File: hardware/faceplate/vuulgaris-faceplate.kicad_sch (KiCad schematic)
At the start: 1 part, among them J1 2x5 SMD box header -- PLACEHO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

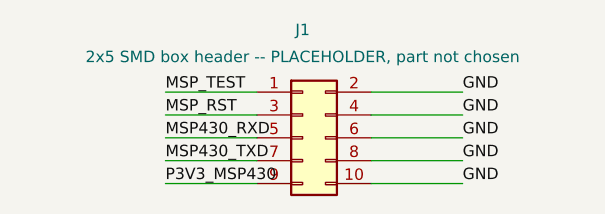
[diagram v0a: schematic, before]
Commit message: faceplate: J1 is the hanxia HX JN2.54-2x5P TP H8.9 (C41376028)
The cable header's placeholder (KiCad's generic SMD box header) is replaced by
a real part. It is Extended: JLC's Basic filter returns no SMD 2x5 box header
at all. Of the SMD ones, this has the most JLC stock (4715) and a drawing with
a recommended land pattern; the runner-up, XFCN BH254VS-10P (C492446), is
10.5mm tall against a 10mm gap. This one seats at 9.60mm.

New footprint IDC-SMD_10P-P2.54_C41376028 in the shared library, from hanxia's
drawing (datasheets/hanxia-HX-JN2.54-2x5P-TP-H8.9.pdf, now in
fetch-datasheets.sh), read at 6x: pads 1.02 x 4.65 on 2.54mm pitch, 11.50
overall (row centres +-3.425); body 20.30 x 8.90; leg tips 10.20 across; key
slot 4.50 wide. Fab carries the body and the leg tips, which is what
panelcheck measures against the cutout. The drawing marks pin 1 only by a
triangle on the key wall, so pin 1 is on the key-side row at that end -- the
same convention as KiCad's DIN 41651 footprint and main-board J12. Still to be
confirmed with a real ribbon before ordering (README section 5).

Board: J1 swapped by a one-off pcbnew script using mkboard.py's rule (pad
centroid on the cutout centre, pad 1 the way J12's lies, on B.Cu) and its
four GND row joins redrawn for the new pads. Diffed against HEAD: J1 and
those four segments are the only changes; the centroid is where it was.

Checked: netcheck 10/10, 0 unintended; boardcheck 0/0/0; DRC 0 errors, 0
warnings (the stock footprint's warning is gone); panelcheck 6 OK -- body and
legs 20.40 x 10.30 in the 24 x 12 cutout, tightest side 0.85mm.
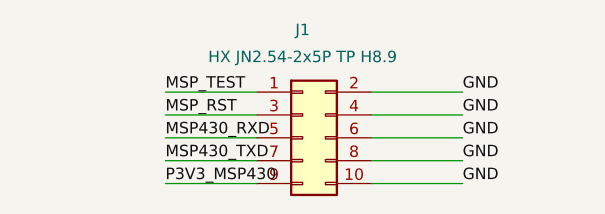
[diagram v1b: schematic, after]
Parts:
- J1: value 2x5 SMD box header -- PLACEHOLDER, part not chosen -> HX JN2.54-2x5P TP H8.9; footprint Connector_IDC:IDC-Header_2x05_P2.54mm_Vertical_SMD -> vuulgaris:IDC-SMD_10P-P2.54_C41376028
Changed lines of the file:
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@@
     (in_bom yes) (on_board yes) (dnp no)
     (property "Reference" "J1" (at 100 88 0) (effects (font (size 1.27 1.27))))
-    (property "Value" "2x5 SMD box header -- PLACEHOLDER, part not chosen" (at 100 91 0) (effects (font (size 1.27 1.27))))
-    (property "Footprint" "Connector_IDC:IDC-Header_2x05_P2.54mm_Vertical_SMD" (at 100 100 0) (effects (font (size 1.27 1.27)) hide))
+    (property "Value" "HX JN2.54-2x5P TP H8.9" (at 100 91 0) (effects (font (size 1.27 1.27))))
+    (property "Footprint" "vuulgaris:IDC-SMD_10P-P2.54_C41376028" (at 100 100 0) (effects (font (size 1.27 1.27)) hide))
     (property "Datasheet" "" (at 100 100 0) (effects (font (size 1.27 1.27)) hide))
     (pin "1")

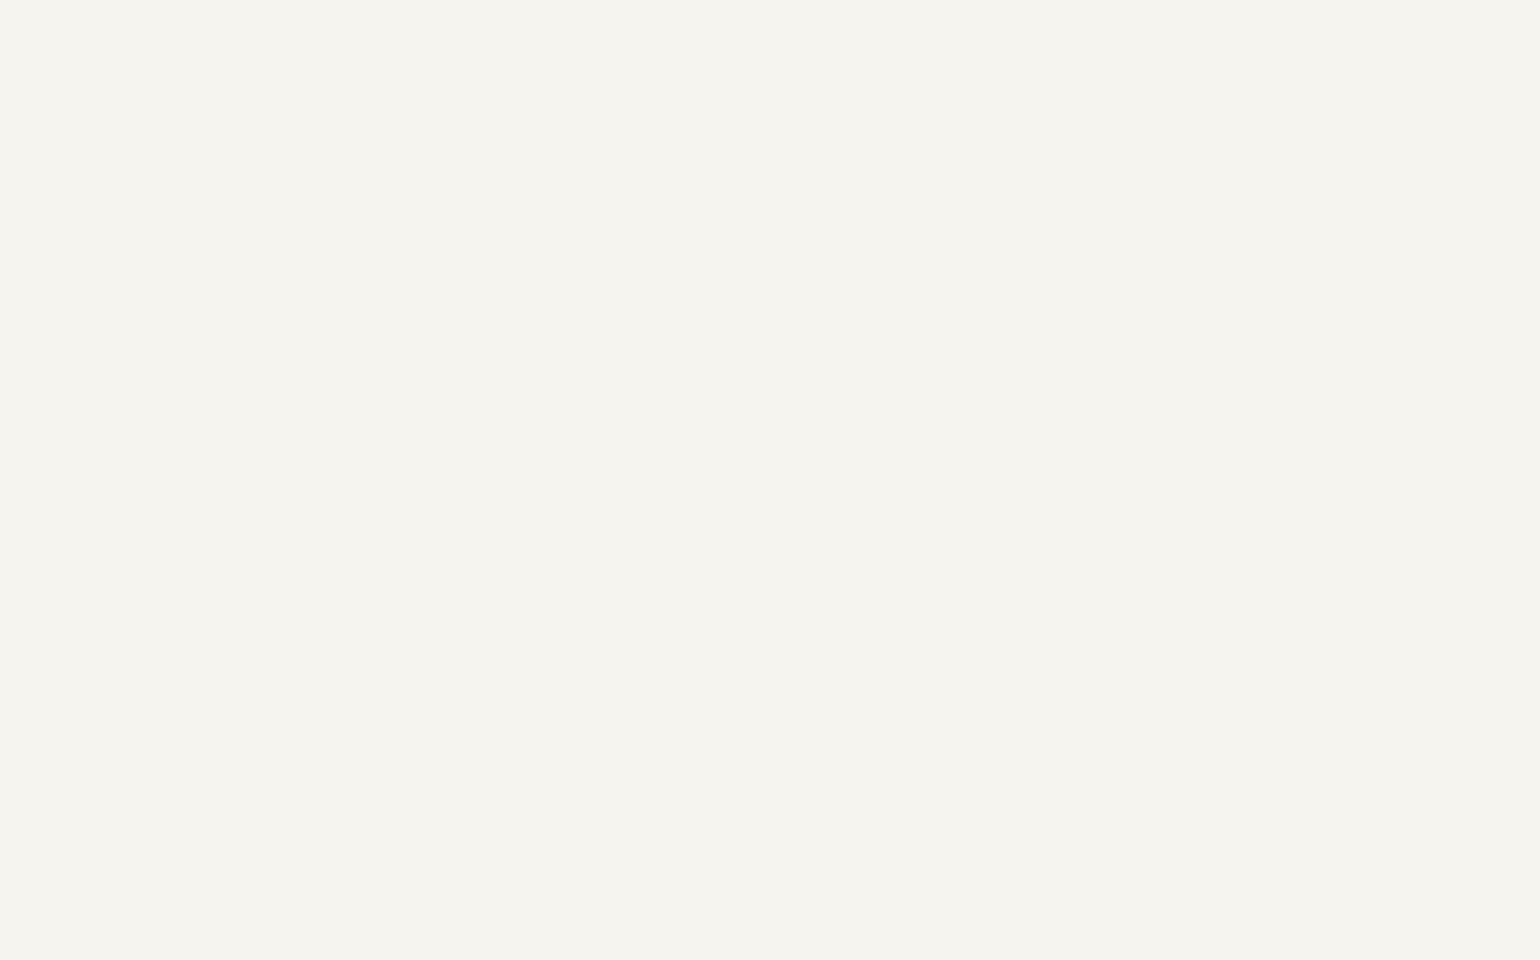
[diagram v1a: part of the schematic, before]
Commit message: faceplate: U1 with its supply, VREG and RST/TEST network
U1 (MSP430FR2675TPT) enters the schematic with the parts TI's reference
circuits call for around its supply and system pins. design.py is now
arranged by block, each saying which figure it came from.

From a TI reference circuit (SLASEO5D):
- C1 10uF + C2 100nF on DVCC/DVSS: section 10.1.1, Figure 10-1. DVCC is
  P3V3_MSP430 straight off the cable; the figure has nothing between supply
  and pin but the two capacitors.
- C3 1uF on VREG (pin 31): section 4, notes under Figure 4-1, "1 uF, with a
  maximum ESR of <=200 mohm".
- R1 47k pull-up + C4 1nF on RST/NMI/SBWTDIO (pin 2): Figure 10-4, the
  Spy-Bi-Wire connection, "upper limit for C1 is 1.1 nF". Required, not just
  tidy: MSP_RST is driven by the main board's MCP23017, high-Z at power-up.
- TEST/SBWTCK (pin 3): nothing. Figure 10-4 wires it straight to the tool;
  Table 7-4, unused TEST: "Open. This pin always has an internal pulldown
  enabled". pin-allocation.md asked for an external pulldown; corrected to
  TI's text in this commit.

Not from a reference circuit: package sizes (0603, 0805 at 1uF and up) follow
the main board's standard. TI's hardware tools guide (SLAU278) was not
fetched; the device datasheet's own Figure 10-4 gives the SBW values for this
part.

Checked: mksch -> netcheck 25/25, 0 unintended, 7 nets. DRC 0/0 and
panelcheck unchanged (the board is not touched). boardcheck parity lists
U1 and C1-C4/R1 as absent from the board -- expected until layout; nothing
is on a net netmap did not ask for.
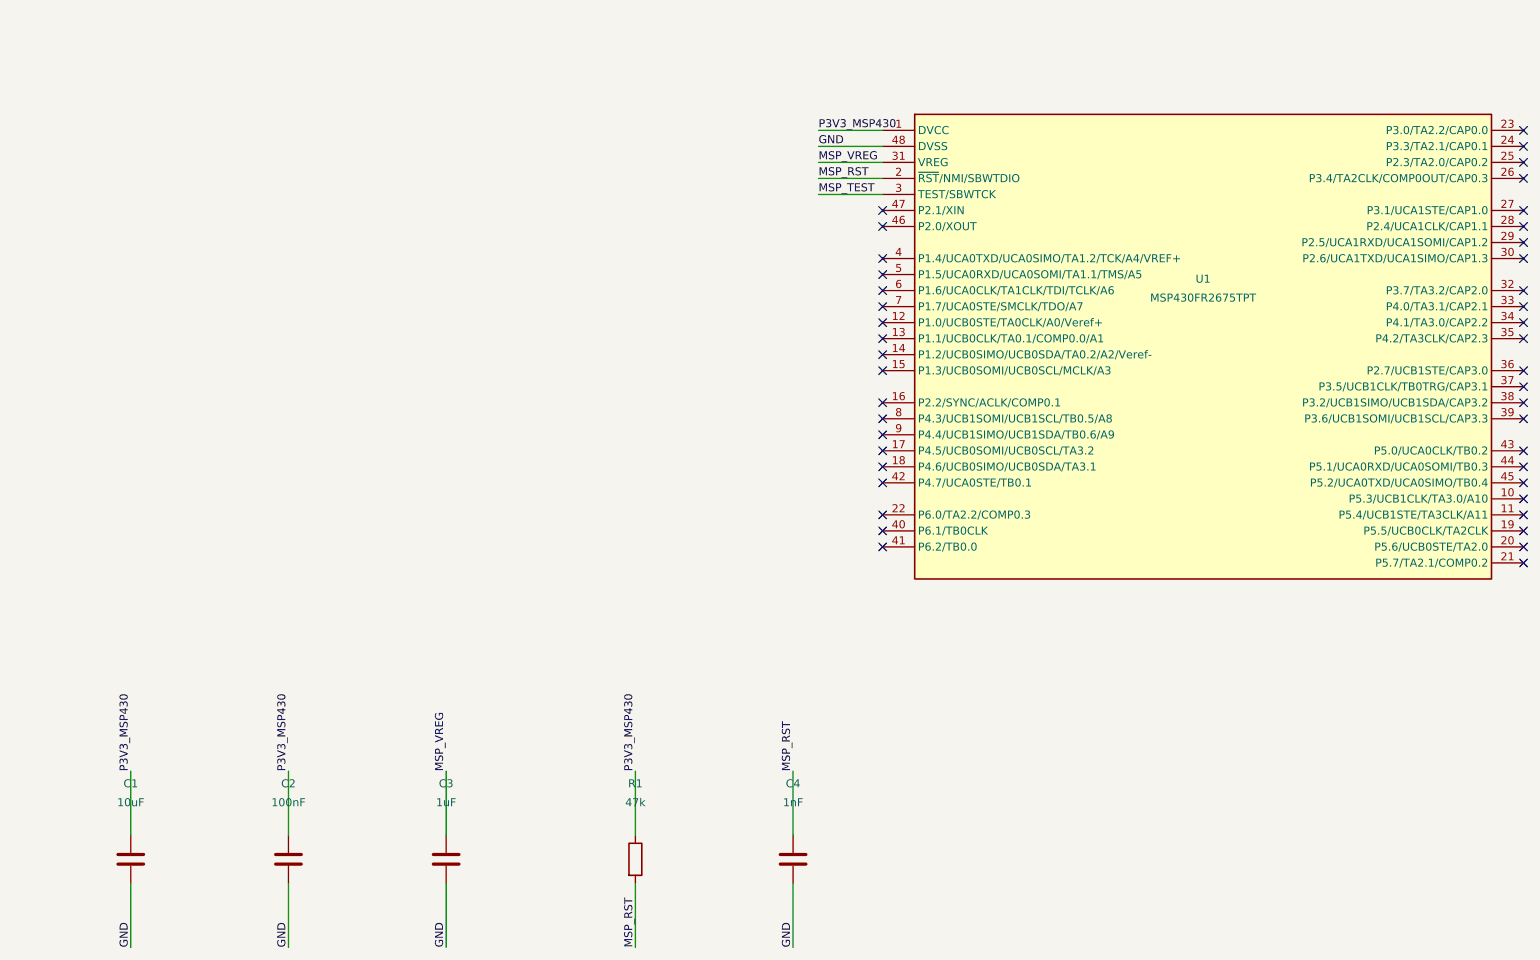
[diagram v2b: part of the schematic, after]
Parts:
- added C1: 10uF, vuulgaris:C0805, symbol vuulgaris:C
- added C2: 100nF, vuulgaris:C0603, symbol vuulgaris:C
- added C3: 1uF, vuulgaris:C0805, symbol vuulgaris:C
- added C4: 1nF, vuulgaris:C0603, symbol vuulgaris:C
- added R1: 47k, vuulgaris:R0603, symbol vuulgaris:R
- added U1: MSP430FR2675TPT, vuulgaris:LQFP-48_7x7mm_P0.5mm_PT0048A, symbol vuulgaris:MSP430FR2675TPT
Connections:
- net GND: now also C1.2, C2.2, C3.2, C4.2, U1.48 (DVSS)
- net MSP_RST: now also C4.1, R1.2, U1.2 (~{RST}/NMI/SBWTDIO)
- net MSP_TEST: now also U1.3 (TEST/SBWTCK)
- net P3V3_MSP430: now also C1.1, C2.1, R1.1, U1.1 (DVCC)
- new net MSP_VREG: C3.1, U1.31 (VREG)
- no-connect marks 0 -> 43
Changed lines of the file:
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@@
 (kicad_sch (version 20221206) (generator eeschema)
   (paper "A1")
+  (symbol (lib_id "vuulgaris:C") (at 160 300 0) (unit 1)
+    (in_bom yes) (on_board yes) (dnp no)
+    (property "Reference" "C1" (at 160 288 0) (effects (font (size 1.27 1.27))))
+    (property "Value" "10uF" (at 160 291 0) (effects (font (size 1.27 1.27))))
+    (property "Footprint" "vuulgaris:C0805" (at 160 300 0) (effects (font (size 1.27 1.27)) hide))
+    (property "Datasheet" "" (at 160 300 0) (effects (font (size 1.27 1.27)) hide))
+    (pin "1")
+    (pin "2")
+  )
+  (symbol (lib_id "vuulgaris:C") (at 185 300 0) (unit 1)
+    (in_bom yes) (on_board yes) (dnp no)
+    (property "Reference" "C2" (at 185 288 0) (effects (font (size 1.27 1.27))))
+    (property "Value" "100nF" (at 185 291 0) (effects (font (size 1.27 1.27))))
+    (property "Footprint" "vuulgaris:C0603" (at 185 300 0) (effects (font (size 1.27 1.27)) hide))
+    (property "Datasheet" "" (at 185 300 0) (effects (font (size 1.27 1.27)) hide))
+    (pin "1")
+    (pin "2")
+  )
+  (symbol (lib_id "vuulgaris:C") (at 210 300 0) (unit 1)
+    (in_bom yes) (on_board yes) (dnp no)
+    (property "Reference" "C3" (at 210 288 0) (effects (font (size 1.27 1.27))))
+    (property "Value" "1uF" (at 210 291 0) (effects (font (size 1.27 1.27))))
+    (property "Footprint" "vuulgaris:C0805" (at 210 300 0) (effects (font (size 1.27 1.27)) hide))
+    (property "Datasheet" "" (at 210 300 0) (effects (font (size 1.27 1.27)) hide))
+    (pin "1")
+    (pin "2")
+  )
+  (symbol (lib_id "vuulgaris:C") (at 265 300 0) (unit 1)
+    (in_bom yes) (on_board yes) (dnp no)
+    (property "Reference" "C4" (at 265 288 0) (effects (font (size 1.27 1.27))))
+    (property "Value" "1nF" (at 265 291 0) (effects (font (size 1.27 1.27))))
+    (property "Footprint" "vuulgaris:C0603" (at 265 300 0) (effects (font (size 1.27 1.27)) hide))
+    (property "Datasheet" "" (at 265 300 0) (effects (font (size 1.27 1.27)) hide))
+    (pin "1")
+    (pin "2")
+  )
   (symbol (lib_id "vuulgaris:Conn_02x05_Odd_Even") (at 100 100 0) (unit 1)
     (in_bom yes) (on_board yes) (dnp no)
@@
     (pin "9")
   )
+  (symbol (lib_id "vuulgaris:R") (at 240 300 0) (unit 1)
+    (in_bom yes) (on_board yes) (dnp no)
+    (property "Reference" "R1" (at 240 288 0) (effects (font (size 1.27 1.27))))
+    (property "Value" "47k" (at 240 291 0) (effects (font (size 1.27 1.27))))
+    (property "Footprint" "vuulgaris:R0603" (at 240 300 0) (effects (font (size 1.27 1.27)) hide))
+    (property "Datasheet" "" (at 240 300 0) (effects (font (size 1.27 1.27)) hide))
+    (pin "1")
+    (pin "2")
+  )
+  (symbol (lib_id "vuulgaris:MSP430FR2675TPT") (at 330 220 0) (unit 1)
+    (in_bom yes) (on_board yes) (dnp no)
+    (property "Reference" "U1" (at 330 208 0) (effects (font (size 1.27 1.27))))
+    (property "Value" "MSP430FR2675TPT" (at 330 211 0) (effects (font (size 1.27 1.27))))
+    (property "Footprint" "vuulgaris:LQFP-48_7x7mm_P0.5mm_PT0048A" (at 330 220 0) (effects (font (size 1.27 1.27)) hide))
+    (property "Datasheet" "" (at 330 220 0) (effects (font (size 1.27 1.27)) hide))
+    (pin "1")
+    (pin "48")
+    (pin "31")
+    (pin "2")
+    (pin "3")
+    (pin "47")
+    (pin "46")
+    (pin "4")
+    (pin "5")
+    (pin "6")
+    (pin "7")
+    (pin "12")
+    (pin "13")
+    (pin "14")
+    (pin "15")
+    (pin "16")
+    (pin "8")
+    (pin "9")
+    (pin "17")
+    (pin "18")
+    (pin "42")
+    (pin "22")
+    (pin "40")
+    (pin "41")
+    (pin "23")
+    (pin "24")
+    (pin "25")
+    (pin "26")
+    (pin "27")
+    (pin "28")
+    (pin "29")
+    (pin "30")
+    (pin "32")
+    (pin "33")
+    (pin "34")
+    (pin "35")
+    (pin "36")
+    (pin "37")
+    (pin "38")
+    (pin "39")
+    (pin "43")
+    (pin "44")
+    (pin "45")
+    (pin "10")
+    (pin "11")
+    (pin "19")
+    (pin "20")
+    (pin "21")
+  )
+  (wire (pts (xy 160.0 296.19) (xy 160.0 286.03)) (stroke (width 0) (type solid)))
+  (wire (pts (xy 160.0 303.81) (xy 160.0 313.97)) (stroke (width 0) (type solid)))
+  (wire (pts (xy 185.0 296.19) (xy 185.0 286.03)) (stroke (width 0) (type solid)))
+  (wire (pts (xy 185.0 303.81) (xy 185.0 313.97)) (stroke (width 0) (type solid)))
+  (wire (pts (xy 210.0 296.19) (xy 210.0 286.03)) (stroke (width 0) (type solid)))
+  (wire (pts (xy 210.0 303.81) (xy 210.0 313.97)) (stroke (width 0) (type solid)))
+  (wire (pts (xy 265.0 296.19) (xy 265.0 286.03)) (stroke (width 0) (type solid)))
+  (wire (pts (xy 265.0 303.81) (xy 265.0 313.97)) (stroke (width 0) (type solid)))
   (wire (pts (xy 94.92 94.92) (xy 84.76 94.92)) (stroke (width 0) (type solid)))
   (wire (pts (xy 107.62 94.92) (xy 117.78 94.92)) (stroke (width 0) (type solid)))
@@
   (wire (pts (xy 94.92 105.08) (xy 84.76 105.08)) (stroke (width 0) (type solid)))
   (wire (pts (xy 107.62 105.08) (xy 117.78 105.08)) (stroke (width 0) (type solid)))
+  (wire (pts (xy 240.0 296.19) (xy 240.0 286.03)) (stroke (width 0) (type solid)))
+  (wire (pts (xy 240.0 303.81) (xy 240.0 313.97)) (stroke (width 0) (type solid)))
+  (wire (pts (xy 279.2 184.44) (xy 269.04 184.44)) (stroke (width 0) (type solid)))
+  (wire (pts (xy 279.2 186.98) (xy 269.04 186.98)) (stroke (width 0) (type solid)))
+  (wire (pts (xy 279.2 189.52) (xy 269.04 189.52)) (stroke (width 0) (type solid)))
+  (wire (pts (xy 279.2 192.06) (xy 269.04 192.06)) (stroke (width 0) (type solid)))
+  (wire (pts (xy 279.2 194.6) (xy 269.04 194.6)) (stroke (width 0) (type solid)))
+  (label "P3V3_MSP430" (at 160.0 286.03 90) (fields_autoplaced)
+    (effects (font (size 1.27 1.27)) (justify left bottom))
+  )
+  (label "GND" (at 160.0 313.97 270) (fields_autoplaced)
+    (effects (font (size 1.27 1.27)) (justify left bottom))
+  )
+  (label "P3V3_MSP430" (at 185.0 286.03 90) (fields_autoplaced)
+    (effects (font (size 1.27 1.27)) (justify left bottom))
+  )
+  (label "GND" (at 185.0 313.97 270) (fields_autoplaced)
+    (effects (font (size 1.27 1.27)) (justify left bottom))
+  )
+  (label "MSP_VREG" (at 210.0 286.03 90) (fields_autoplaced)
+    (effects (font (size 1.27 1.27)) (justify left bottom))
+  )
+  (label "GND" (at 210.0 313.97 270) (fields_autoplaced)
+    (effects (font (size 1.27 1.27)) (justify left bottom))
+  )
+  (label "MSP_RST" (at 265.0 286.03 90) (fields_autoplaced)
+    (effects (font (size 1.27 1.27)) (justify left bottom))
+  )
+  (label "GND" (at 265.0 313.97 270) (fields_autoplaced)
+    (effects (font (size 1.27 1.27)) (justify left bottom))
+  )
   (label "MSP_TEST" (at 84.76 94.92 180) (fields_autoplaced)
     (effects (font (size 1.27 1.27)) (justify left bottom))
@@
     (effects (font (size 1.27 1.27)) (justify left bottom))
   )
+  (label "P3V3_MSP430" (at 240.0 286.03 90) (fields_autoplaced)
+    (effects (font (size 1.27 1.27)) (justify left bottom))
+  )
+  (label "MSP_RST" (at 240.0 313.97 270) (fields_autoplaced)
+    (effects (font (size 1.27 1.27)) (justify left bottom))
+  )
+  (label "P3V3_MSP430" (at 269.04 184.44 180) (fields_autoplaced)
+    (effects (font (size 1.27 1.27)) (justify left bottom))
+  )
+  (label "GND" (at 269.04 186.98 180) (fields_autoplaced)
+    (effects (font (size 1.27 1.27)) (justify left bottom))
+  )
+  (label "MSP_VREG" (at 269.04 189.52 180) (fields_autoplaced)
+    (effects (font (size 1.27 1.27)) (justify left bottom))
+  )
+  (label "MSP_RST" (at 269.04 192.06 180) (fields_autoplaced)
+    (effects (font (size 1.27 1.27)) (justify left bottom))
+  )
+  (label "MSP_TEST" (at 269.04 194.6 180) (fields_autoplaced)
+    (effects (font (size 1.27 1.27)) (justify left bottom))
+  )
+  (no_connect (at 279.2 197.14))
+  (no_connect (at 279.2 199.68))
+  (no_connect (at 279.2 204.76))
+  (no_connect (at 279.2 207.3))
+  (no_connect (at 279.2 209.84))
+  (no_connect (at 279.2 212.38))
+  (no_connect (at 279.2 214.92))
+  (no_connect (at 279.2 217.46))
+  (no_connect (at 279.2 220.0))
+  (no_connect (at 279.2 222.54))
+  (no_connect (at 279.2 227.62))
+  (no_connect (at 279.2 230.16))
+  (no_connect (at 279.2 232.7))
+  (no_connect (at 279.2 235.24))
+  (no_connect (at 279.2 237.78))
+  (no_connect (at 279.2 240.32))
+  (no_connect (at 279.2 245.4))
+  (no_connect (at 279.2 247.94))
+  (no_connect (at 279.2 250.48))
+  (no_connect (at 380.8 184.44))
+  (no_connect (at 380.8 186.98))
+  (no_connect (at 380.8 189.52))
+  (no_connect (at 380.8 192.06))
+  (no_connect (at 380.8 197.14))
+  (no_connect (at 380.8 199.68))
+  (no_connect (at 380.8 202.22))
+  (no_connect (at 380.8 204.76))
+  (no_connect (at 380.8 209.84))
+  (no_connect (at 380.8 212.38))
+  (no_connect (at 380.8 214.92))
+  (no_connect (at 380.8 217.46))
+  (no_connect (at 380.8 222.54))
+  (no_connect (at 380.8 225.08))
+  (no_connect (at 380.8 227.62))
+  (no_connect (at 380.8 230.16))
+  (no_connect (at 380.8 235.24))
+  (no_connect (at 380.8 237.78))
+  (no_connect (at 380.8 240.32))
+  (no_connect (at 380.8 242.86))
+  (no_connect (at 380.8 245.4))
+  (no_connect (at 380.8 247.94))
+  (no_connect (at 380.8 250.48))
+  (no_connect (at 380.8 253.02))
   (sheet_instances (path "/" (page "1")))
 )
